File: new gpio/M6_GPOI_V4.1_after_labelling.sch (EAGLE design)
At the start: 36 parts, among them IC4 LT1161, Q5 16MHz, Q8 16MHz, U3 MCP2515, U4 ATMEGA328P_PDIP, X2 MABC96R

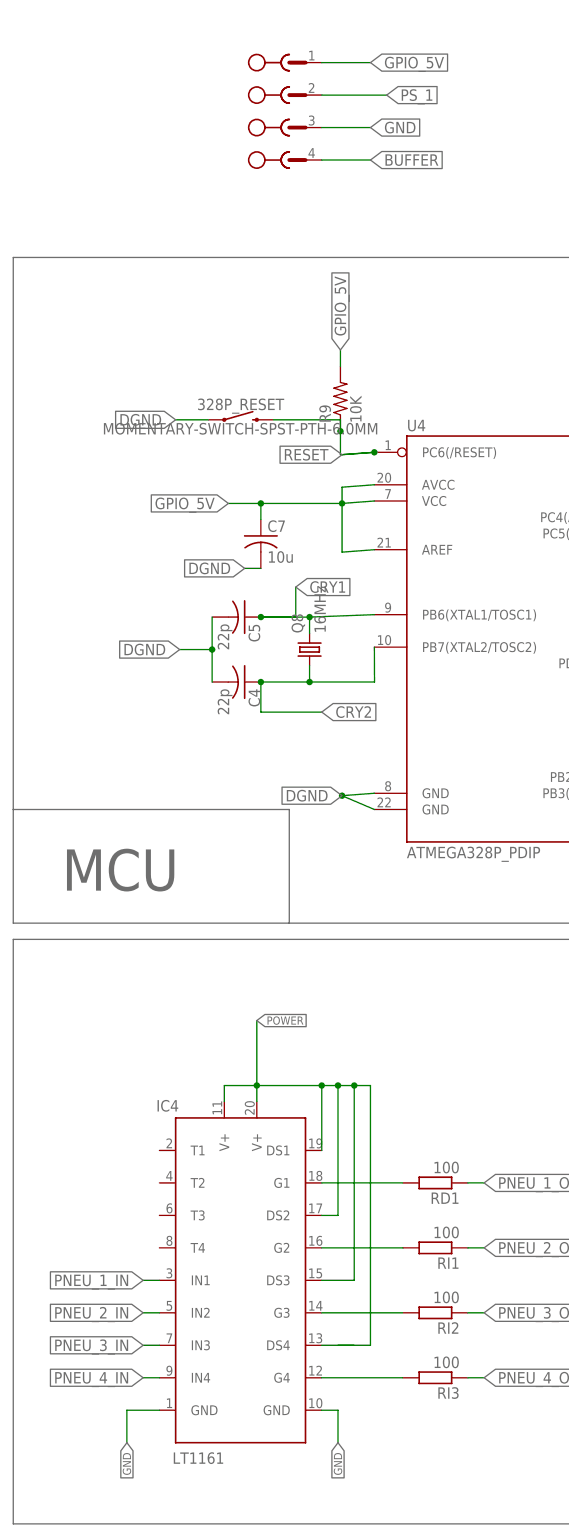
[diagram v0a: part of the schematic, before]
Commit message: updated with dimensions
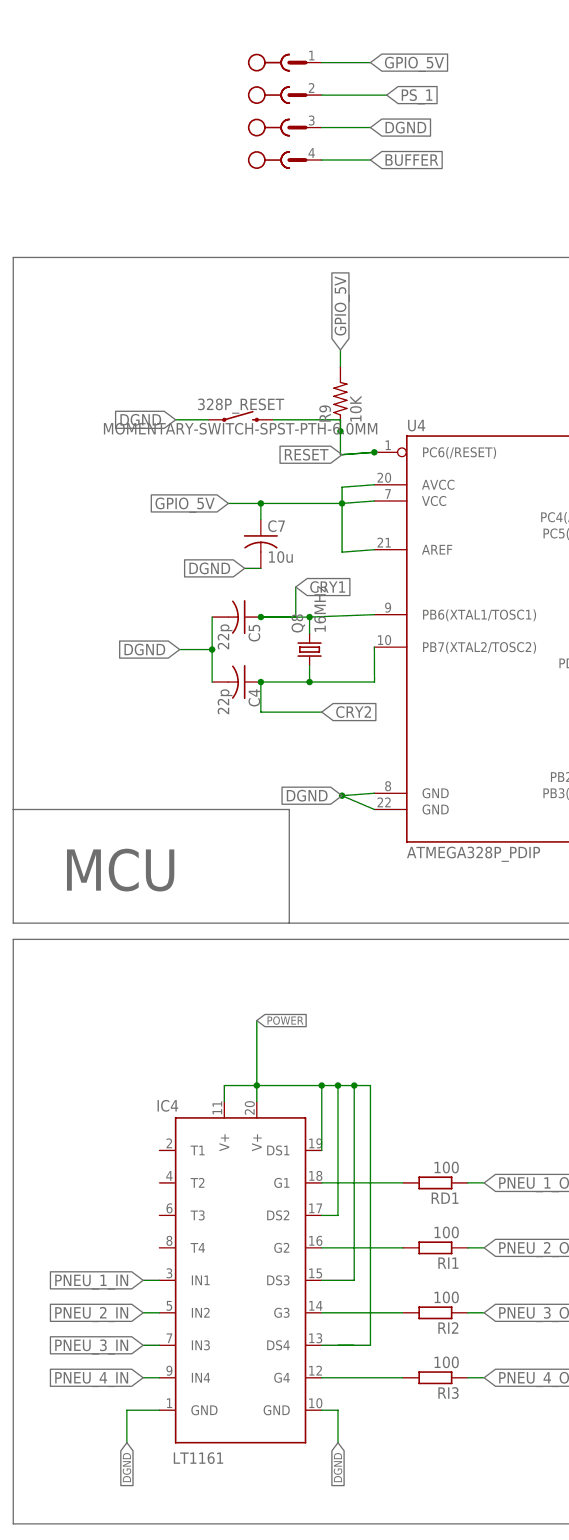
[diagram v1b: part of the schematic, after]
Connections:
- removed net GND: IC4.GND@1, IC4.GND@2, PS-3.1
- net DGND: now also IC4.GND@1, IC4.GND@2, PS-3.1
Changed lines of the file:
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@@
 <junction x="582.93" y="28.448"/>
+</segment>
+<segment>
+<wire x1="375.92" y1="-172.72" x2="378.46" y2="-172.72" width="0.1524" layer="91"/>
+<wire x1="378.46" y1="-172.72" x2="378.46" y2="-177.8" width="0.1524" layer="91"/>
+<label x="378.46" y="-177.8" size="1.27" layer="95" rot="R270" xref="yes"/>
+<pinref part="IC4" gate="G$1" pin="GND@2"/>
+</segment>
+<segment>
+<wire x1="350.52" y1="-172.72" x2="345.44" y2="-172.72" width="0.1524" layer="91"/>
+<wire x1="345.44" y1="-172.72" x2="345.44" y2="-177.8" width="0.1524" layer="91"/>
+<label x="345.44" y="-177.8" size="1.27" layer="95" rot="R270" xref="yes"/>
+<pinref part="IC4" gate="G$1" pin="GND@1"/>
+</segment>
+<segment>
+<pinref part="PS" gate="-3" pin="1"/>
+<wire x1="375.92" y1="27.94" x2="383.54" y2="27.94" width="0.1524" layer="91"/>
+<label x="383.54" y="27.94" size="1.778" layer="95" xref="yes"/>
 </segment>
 </net>
@@
 <net name="PWM1" class="0">
 <segment>
-<wire x1="432.435" y1="-60.96" x2="452.12" y2="-60.96" width="0.1524" layer="91"/>
-<label x="452.12" y="-60.96" size="1.778" layer="95" xref="yes"/>
-<pinref part="U4" gate="G$1" pin="PD6(AIN0)"/>
-<wire x1="432.409953125" y1="-60.9606375" x2="432.435" y2="-60.96" width="0.1524" layer="91"/>
-</segment>
-<segment>
 <wire x1="584.2" y1="-165.1" x2="571.5" y2="-165.1" width="0.1524" layer="91"/>
 <label x="571.5" y="-165.1" size="1.778" layer="95" rot="R180" xref="yes"/>
@@
 <junction x="584.2" y="-165.1"/>
 </segment>
+<segment>
+<wire x1="432.435" y1="-60.96" x2="452.12" y2="-60.96" width="0.1524" layer="91"/>
+<label x="452.12" y="-60.96" size="1.778" layer="95" xref="yes"/>
+<pinref part="U4" gate="G$1" pin="PD6(AIN0)"/>
+<wire x1="432.409953125" y1="-60.9606375" x2="432.435" y2="-60.96" width="0.1524" layer="91"/>
+</segment>
 </net>
 <net name="PWM2" class="0">
-<segment>
-<pinref part="U4" gate="G$1" pin="PD7(AIN1)"/>
-<wire x1="432.435" y1="-63.5" x2="441.96" y2="-63.5" width="0.1524" layer="91"/>
-<label x="441.96" y="-63.5" size="1.778" layer="95" xref="yes"/>
-<wire x1="432.409953125" y1="-63.5006375" x2="432.435" y2="-63.5" width="0.1524" layer="91"/>
-</segment>
 <segment>
 <wire x1="584.2" y1="-162.56" x2="571.5" y2="-162.56" width="0.1524" layer="91"/>
@@
 <junction x="601.98" y="-162.56"/>
 <junction x="584.2" y="-162.56"/>
+</segment>
+<segment>
+<pinref part="U4" gate="G$1" pin="PD7(AIN1)"/>
+<wire x1="432.435" y1="-63.5" x2="441.96" y2="-63.5" width="0.1524" layer="91"/>
+<label x="441.96" y="-63.5" size="1.778" layer="95" xref="yes"/>
+<wire x1="432.409953125" y1="-63.5006375" x2="432.435" y2="-63.5" width="0.1524" layer="91"/>
 </segment>
 </net>
@@
 </segment>
 </net>
-<net name="GND" class="0">
-<segment>
-<wire x1="375.92" y1="-172.72" x2="378.46" y2="-172.72" width="0.1524" layer="91"/>
-<wire x1="378.46" y1="-172.72" x2="378.46" y2="-177.8" width="0.1524" layer="91"/>
-<label x="378.46" y="-177.8" size="1.27" layer="95" rot="R270" xref="yes"/>
-<pinref part="IC4" gate="G$1" pin="GND@2"/>
-</segment>
-<segment>
-<wire x1="350.52" y1="-172.72" x2="345.44" y2="-172.72" width="0.1524" layer="91"/>
-<wire x1="345.44" y1="-172.72" x2="345.44" y2="-177.8" width="0.1524" layer="91"/>
-<label x="345.44" y="-177.8" size="1.27" layer="95" rot="R270" xref="yes"/>
-<pinref part="IC4" gate="G$1" pin="GND@1"/>
-</segment>
-<segment>
-<pinref part="PS" gate="-3" pin="1"/>
-<wire x1="375.92" y1="27.94" x2="383.54" y2="27.94" width="0.1524" layer="91"/>
-<label x="383.54" y="27.94" size="1.778" layer="95" xref="yes"/>
-</segment>
-</net>

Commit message: gpio with nobi's changes
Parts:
- removed C1: (no value), capacitor-wima:C2,5-3
- removed D1: 5v, diode:ZENER-DIODEZD-10
- removed PS: MSTBA4, con-phoenix-508:MSTBA4
- removed R18: (no value), rcl:R-EU_M0805
- removed R3: 2.2k, SparkFun-Resistors:RESISTORAXIAL-0.3
- removed R8: 0.732k, SparkFun-Resistors:RESISTORAXIAL-0.3
- added SL1: (no value), con-amp-quick:MA03
- renumbered LED3 to GPIO_5V, LED5 to CAN_STATUS
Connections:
- net CRY1 renamed CRY_N
- net CRY2 renamed CRY_P
- net N$10 renamed C_N
- net N$9 renamed C_P
- removed net BUFFER: PS-4.1, U4.PC2(ADC2)
- removed net GPIO_5V: C1.1, C7.1, C9.1, J2.2, PS-1.1, R1.1, R18.1, R3.1, R7.2, R8.2, R9.2, U$3.VDD, U3P.VDD, U4.AREF, U4.AVCC, U4.VCC
- removed net N$21: D1.C, R18.2
- net DGND: now also SL1.2; no longer C1.2, D1.A, J2.4, J2.6, J2.8, PS-3.1, R8.1
- net GPIO_POWER: now also C7.1, C9.1, J2.2, R1.1, R7.2, R9.2, SL1.3, U$3.VDD, U3P.VDD, U4.AREF, U4.AVCC, U4.VCC; no longer R3.2
- net INT_1: now also U4.PC2(ADC2)
- net PS_1: now also SL1.1; no longer PS-2.1
- net PWM1: now also U4.PD7(AIN1); no longer U4.PD6(AIN0)
- net PWM2: now also U4.PD6(AIN0); no longer U4.PD7(AIN1)
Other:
- note removed: "Over Voltage Protect"

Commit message: FINAL BY LK WITHOUT LABELLING
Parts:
- removed C7: 10u, resistor:C-US025-024X044
- removed CAN_STATUS, GPIO_5V: (no value), eagle-ltspice:LED_ELD260
- removed R1: 10K, SparkFun-Resistors:0.75OHM-0805-1/4W-1%
- removed R4, R7: 0.2k, adafruit:R-US_R0603
- removed R9: 10K, rcl:R-US_0204/2V
- added C1, C2: 10u, adafruit:C-US025-050X050
- added PWR, PWR1: (no value), led:LED5MM
- added R2, R24: 1k, rcl:R-EU_M0805
- added RD2, RD3: 10K, rcl:R-EU_M0805
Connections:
- removed net N$4: GPIO_5V.A, R7.1
- new net N$31: PWR.A, R24.1
- net CAN_STAT_1: now also R2.2; no longer R4.1
- net DGND: now also C1.2, C2.2, PWR.C, PWR1.C; no longer C7.2, CAN_STATUS.C, GPIO_5V.C
- net GPIO_POWER: now also C1.1, C2.1, R24.2, RD2.2, RD3.1; no longer C7.1, R1.1, R7.2, R9.2
- net N$1: now also PWR1.A, R2.1; no longer CAN_STATUS.A, R4.2
- net N$8: now also RD2.1; no longer R1.2
- net PNEU_1_IN: now also IC4.IN4, U4.PC1(ADC1); no longer IC4.IN1, U4.PC5(ADC5/SCL)
- net PNEU_1_OUT: now also RI3.1; no longer RD1.1
- net PNEU_2_IN: now also IC4.IN3, U4.PC3(ADC3); no longer IC4.IN2, U4.PC0(ADC0)
- net PNEU_2_OUT: now also RI2.1; no longer RI1.1
- net PNEU_3_IN: now also IC4.IN2, U4.PC4(ADC4/SDA); no longer IC4.IN3, U4.PD0(RXD)
- net PNEU_3_OUT: now also RI1.1; no longer RI2.1
- net PNEU_4_IN: now also IC4.IN1, U4.PC5(ADC5/SCL); no longer IC4.IN4, U4.PD5(T1)
- net PNEU_4_OUT: now also RD1.1; no longer RI3.1
- net PS_1: now also U4.PC0(ADC0); no longer U4.PC1(ADC1)
- net PWM3: now also U4.PD5(T1); no longer U4.PD4(XCK/T0)
- net PWM4: now also U4.PD4(XCK/T0); no longer U4.PD3(INT1)
- net PWM5: now also U4.PD3(INT1); no longer U4.PD2(INT0)
- net PWM6: now also U4.PD2(INT0); no longer U4.PD1(TXD)
- net PWM7: now also U4.PD1(TXD); no longer U4.PC3(ADC3)
- net PWM8: now also U4.PD0(RXD); no longer U4.PC4(ADC4/SDA)
- net RESET: now also RD3.2; no longer R9.1

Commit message: final from lk without labelling
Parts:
- removed PWR, PWR1: (no value), led:LED5MM
- added LED1, LED7: (no value), led:LEDCHIPLED_0805
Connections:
- removed net CAN_N: X2-A10.S, X2-B10.S, X2-C10.S
- removed net CAN_P: X2-A9.S, X2-B9.S, X2-C9.S
- removed net CAN_SCK_M: X2-A5.S, X2-B5.S, X2-C5.S
- removed net CUSTOMPIN1_M: X2-A15.S, X2-B15.S, X2-C15.S
- removed net INT_2: X2-A8.S, X2-B8.S, X2-C8.S
- removed net MOSI_M: X2-A6.S, X2-B6.S, X2-C6.S
- net DGND: now also LED1.C, LED7.C; no longer PWR.C, PWR1.C
- net N$1: now also LED7.A; no longer PWR1.A
- net N$31: now also LED1.A; no longer PWR.A
- net PNEU_1_IN: now also IC4.IN1, U4.PC5(ADC5/SCL); no longer IC4.IN4, U4.PC1(ADC1)
- net PNEU_1_OUT: now also RD1.1; no longer RI3.1
- net PNEU_2_IN: now also IC4.IN2, U4.PC4(ADC4/SDA); no longer IC4.IN3, U4.PC3(ADC3)
- net PNEU_2_OUT: now also RI1.1; no longer RI2.1
- net PNEU_3_IN: now also IC4.IN3, U4.PC3(ADC3); no longer IC4.IN2, U4.PC4(ADC4/SDA)
- net PNEU_3_OUT: now also RI2.1; no longer RI1.1
- net PNEU_4_IN: now also IC4.IN4, U4.PC1(ADC1); no longer IC4.IN1, U4.PC5(ADC5/SCL)
- net PNEU_4_OUT: now also RI3.1; no longer RD1.1
- net PWM1: now also U4.PD0(RXD); no longer U4.PD7(AIN1)
- net PWM2: now also U4.PD1(TXD); no longer U4.PD6(AIN0)
- net PWM3: now also U4.PD2(INT0); no longer U4.PD5(T1)
- net PWM4: now also U4.PD3(INT1); no longer U4.PD4(XCK/T0)
- net PWM5: now also U4.PD4(XCK/T0); no longer U4.PD3(INT1)
- net PWM6: now also U4.PD5(T1); no longer U4.PD2(INT0)
- net PWM7: now also U4.PD6(AIN0); no longer U4.PD1(TXD)
- net PWM8: now also U4.PD7(AIN1); no longer U4.PD0(RXD)
